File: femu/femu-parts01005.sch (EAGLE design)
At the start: 54 parts, among them IC1 ESP32-QFN_5X5, IC3 FT230XQ

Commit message: Updating part names, and cleaning up + filling in MPN attributes
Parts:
- ANT1: MPN (none) -> W3008
- C17: MPN GRM022R60G104ME15L -> GRM022R60G104ME15L
- IC3: MPN (none) -> FT230XQ-R
- LDO1: MPN (none) -> NCP167AFCT330T2G
- renumbered U$11 to ANT1, U$33 to LDO1
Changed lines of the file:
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@@
 <part name="U$22" library="microbuilder" deviceset="GND" device=""/>
 <part name="C17" library="parts_01005" deviceset="CAPACITOR" device="" value="0.1uF">
-<attribute name="MPN" value=" GRM022R60G104ME15L "/>
+<attribute name="MPN" value="GRM022R60G104ME15L"/>
 </part>
 <part name="U$21" library="microbuilder" deviceset="GND" device=""/>
@@
 <part name="U$9" library="microbuilder" deviceset="3.3V" device=""/>
 <part name="FRAME2" library="SparkFun-Aesthetics" deviceset="FRAME-LETTER" device="NO_PACKAGE"/>
-<part name="U$11" library="bar_antenna" deviceset="PULSE_ANT_2.4GHZ" device=""/>
+<part name="ANT1" library="bar_antenna" deviceset="PULSE_ANT_2.4GHZ" device="">
+<attribute name="MPN" value="W3008"/>
+</part>
 <part name="U$23" library="microbuilder" deviceset="GND" device=""/>
 <part name="U$24" library="microbuilder" deviceset="GND" device=""/>
@@
 <part name="U$44" library="microbuilder" deviceset="GND" device=""/>
 <part name="U$2" library="microbuilder" deviceset="VIN" device=""/>
-<part name="IC3" library="ftdichip" library_urn="urn:adsk.eagle:library:231" deviceset="FT230X" device="Q" package3d_urn="urn:adsk.eagle:package:14017/1"/>
+<part name="IC3" library="ftdichip" library_urn="urn:adsk.eagle:library:231" deviceset="FT230X" device="Q" package3d_urn="urn:adsk.eagle:package:14017/1">
+<attribute name="MPN" value="FT230XQ-R"/>
+</part>
 <part name="R8" library="parts_0201" deviceset="RESISTOR_0201" device="" value="27">
 <attribute name="MPN" value="ERJ-1GNF27R0C"/>
@@
 <part name="FID5" library="adafruit" deviceset="FIDUCIAL" device=""/>
 <part name="FID6" library="adafruit" deviceset="FIDUCIAL" device=""/>
-<part name="U$33" library="onsemi" deviceset="NCP167AFCT330T2G" device=""/>
+<part name="LDO1" library="onsemi" deviceset="NCP167AFCT330T2G" device="">
+<attribute name="MPN" value="NCP167AFCT330T2G"/>
+</part>
 <part name="C2" library="parts_0201" deviceset="CAPACITOR_0201" device="" value="1uF">
 <attribute name="MPN" value="CL03A105KQ3CSNH"/>
@@
 <attribute name="VALUE" x="224.536" y="150.876" size="1.27" layer="96"/>
 </instance>
-<instance part="U$11" gate="G$1" x="38.1" y="132.08" smashed="yes" rot="R180"/>
+<instance part="ANT1" gate="G$1" x="38.1" y="132.08" smashed="yes" rot="R180">
+<attribute name="MPN" x="38.1" y="132.08" size="1.778" layer="96" rot="R180" display="off"/>
+</instance>
 <instance part="U$23" gate="G$1" x="10.16" y="134.62" smashed="yes" rot="R270">
 <attribute name="VALUE" x="7.62" y="136.144" size="1.27" layer="96" rot="R270"/>
@@
 </segment>
 <segment>
-<pinref part="U$11" gate="G$1" pin="3"/>
+<pinref part="ANT1" gate="G$1" pin="3"/>
 <pinref part="U$23" gate="G$1" pin="GND"/>
 <wire x1="12.7" y1="134.62" x2="20.32" y2="134.62" width="0.1524" layer="91"/>
 </segment>
 <segment>
-<pinref part="U$11" gate="G$1" pin="2"/>
+<pinref part="ANT1" gate="G$1" pin="2"/>
 <pinref part="U$24" gate="G$1" pin="GND"/>
 <wire x1="43.18" y1="134.62" x2="48.26" y2="134.62" width="0.1524" layer="91"/>
@@
 <wire x1="58.42" y1="129.54" x2="58.42" y2="127" width="0.1524" layer="91"/>
 <pinref part="R6" gate="G$1" pin="2"/>
-<pinref part="U$11" gate="G$1" pin="1"/>
+<pinref part="ANT1" gate="G$1" pin="1"/>
 <wire x1="58.42" y1="129.54" x2="43.18" y2="129.54" width="0.1524" layer="91"/>
 <wire x1="43.18" y1="129.54" x2="43.18" y2="132.08" width="0.1524" layer="91"/>
@@
 <attribute name="DESIGNER" x="170.434" y="11.176" size="2.7432" layer="94" font="vector"/>
 </instance>
-<instance part="U$33" gate="G$1" x="124.46" y="111.76" smashed="yes"/>
+<instance part="LDO1" gate="G$1" x="124.46" y="111.76" smashed="yes">
+<attribute name="MPN" x="124.46" y="111.76" size="1.778" layer="96" display="off"/>
+</instance>
 <instance part="C2" gate="G$1" x="104.14" y="111.76" smashed="yes" rot="R180">
 <attribute name="NAME" x="101.6" y="109.22" size="1.27" layer="95" font="vector" rot="R180"/>
@@
 <segment>
 <pinref part="C3" gate="G$1" pin="P$1"/>
-<pinref part="U$33" gate="G$1" pin="B2/GND"/>
+<pinref part="LDO1" gate="G$1" pin="B2/GND"/>
 <wire x1="144.78" y1="106.68" x2="144.78" y2="93.98" width="0.1524" layer="91"/>
 <wire x1="144.78" y1="93.98" x2="129.54" y2="93.98" width="0.1524" layer="91"/>
@@
 <net name="3.3V" class="0">
 <segment>
-<pinref part="U$33" gate="G$1" pin="A2/OUT"/>
+<pinref part="LDO1" gate="G$1" pin="A2/OUT"/>
 <pinref part="U$34" gate="G$1" pin="3.3V"/>
 <wire x1="129.54" y1="129.54" x2="129.54" y2="132.08" width="0.1524" layer="91"/>
@@
 <net name="VIN" class="0">
 <segment>
-<pinref part="U$33" gate="G$1" pin="A1/IN"/>
+<pinref part="LDO1" gate="G$1" pin="A1/IN"/>
 <pinref part="U$36" gate="G$1" pin="VIN"/>
 <wire x1="119.38" y1="129.54" x2="119.38" y2="132.08" width="0.1524" layer="91"/>
@@
 <wire x1="104.14" y1="114.3" x2="104.14" y2="132.08" width="0.1524" layer="91"/>
 <junction x="104.14" y="132.08"/>
-<pinref part="U$33" gate="G$1" pin="B1/EN"/>
+<pinref part="LDO1" gate="G$1" pin="B1/EN"/>
 <wire x1="119.38" y1="93.98" x2="109.22" y2="93.98" width="0.1524" layer="91"/>
 <wire x1="109.22" y1="93.98" x2="109.22" y2="132.08" width="0.1524" layer="91"/>
@@
 <attribute name="NAME" x="81.28" y="135.89" size="1.778" layer="95" rot="R180"/>
 <attribute name="VALUE" x="81.28" y="162.56" size="1.778" layer="96" rot="R180"/>
+<attribute name="MPN" x="68.58" y="147.32" size="1.778" layer="96" rot="R180" display="off"/>
 </instance>
 <instance part="R8" gate="G$1" x="68.58" y="63.5" smashed="yes">

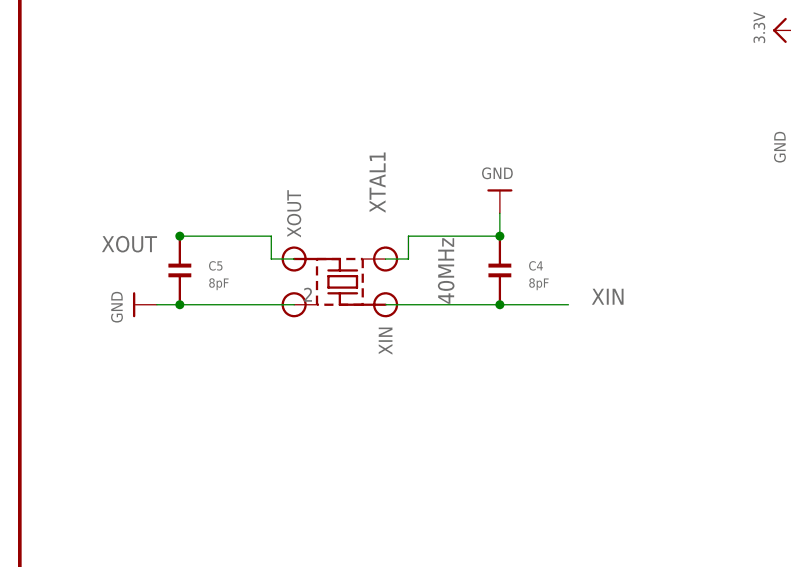
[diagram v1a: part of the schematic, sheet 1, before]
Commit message: XTAL should be using 10pF caps, not 8pF. Fixed
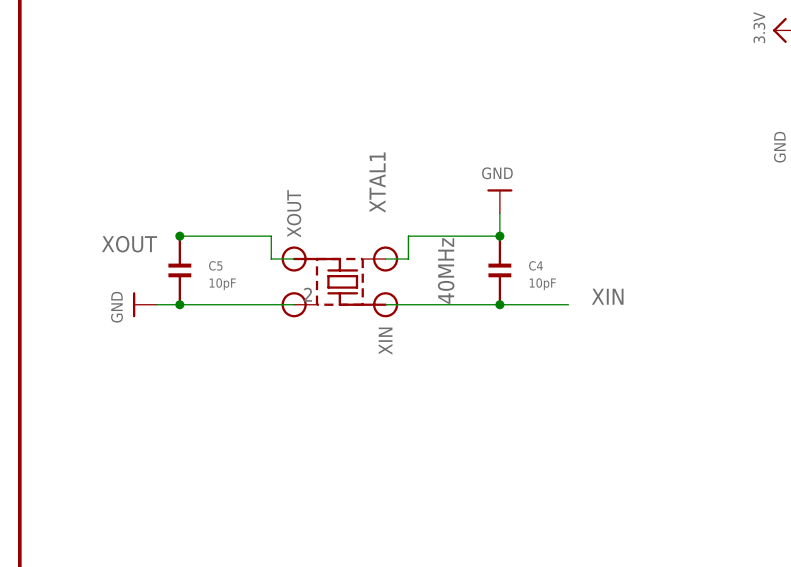
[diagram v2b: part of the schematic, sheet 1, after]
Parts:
- C4, C5: value 8pF -> 10pF; MPN GRM0335C1H8R0DA01D -> CC0201JRNPO9BN100
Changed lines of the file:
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@@
 <attribute name="MPN" value="FA-128 40.0000MF10Z-K3"/>
 </part>
-<part name="C4" library="parts_0201" deviceset="CAPACITOR_0201" device="" value="8pF">
-<attribute name="MPN" value="GRM0335C1H8R0DA01D"/>
+<part name="C4" library="parts_0201" deviceset="CAPACITOR_0201" device="" value="10pF">
+<attribute name="MPN" value="CC0201JRNPO9BN100"/>
 </part>
-<part name="C5" library="parts_0201" deviceset="CAPACITOR_0201" device="" value="8pF">
-<attribute name="MPN" value="GRM0335C1H8R0DA01D"/>
+<part name="C5" library="parts_0201" deviceset="CAPACITOR_0201" device="" value="10pF">
+<attribute name="MPN" value="CC0201JRNPO9BN100"/>
 </part>
 <part name="U$7" library="microbuilder" deviceset="GND" device=""/>
